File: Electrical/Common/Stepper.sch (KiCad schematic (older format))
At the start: 12 parts, among them Q301 FDC6420C

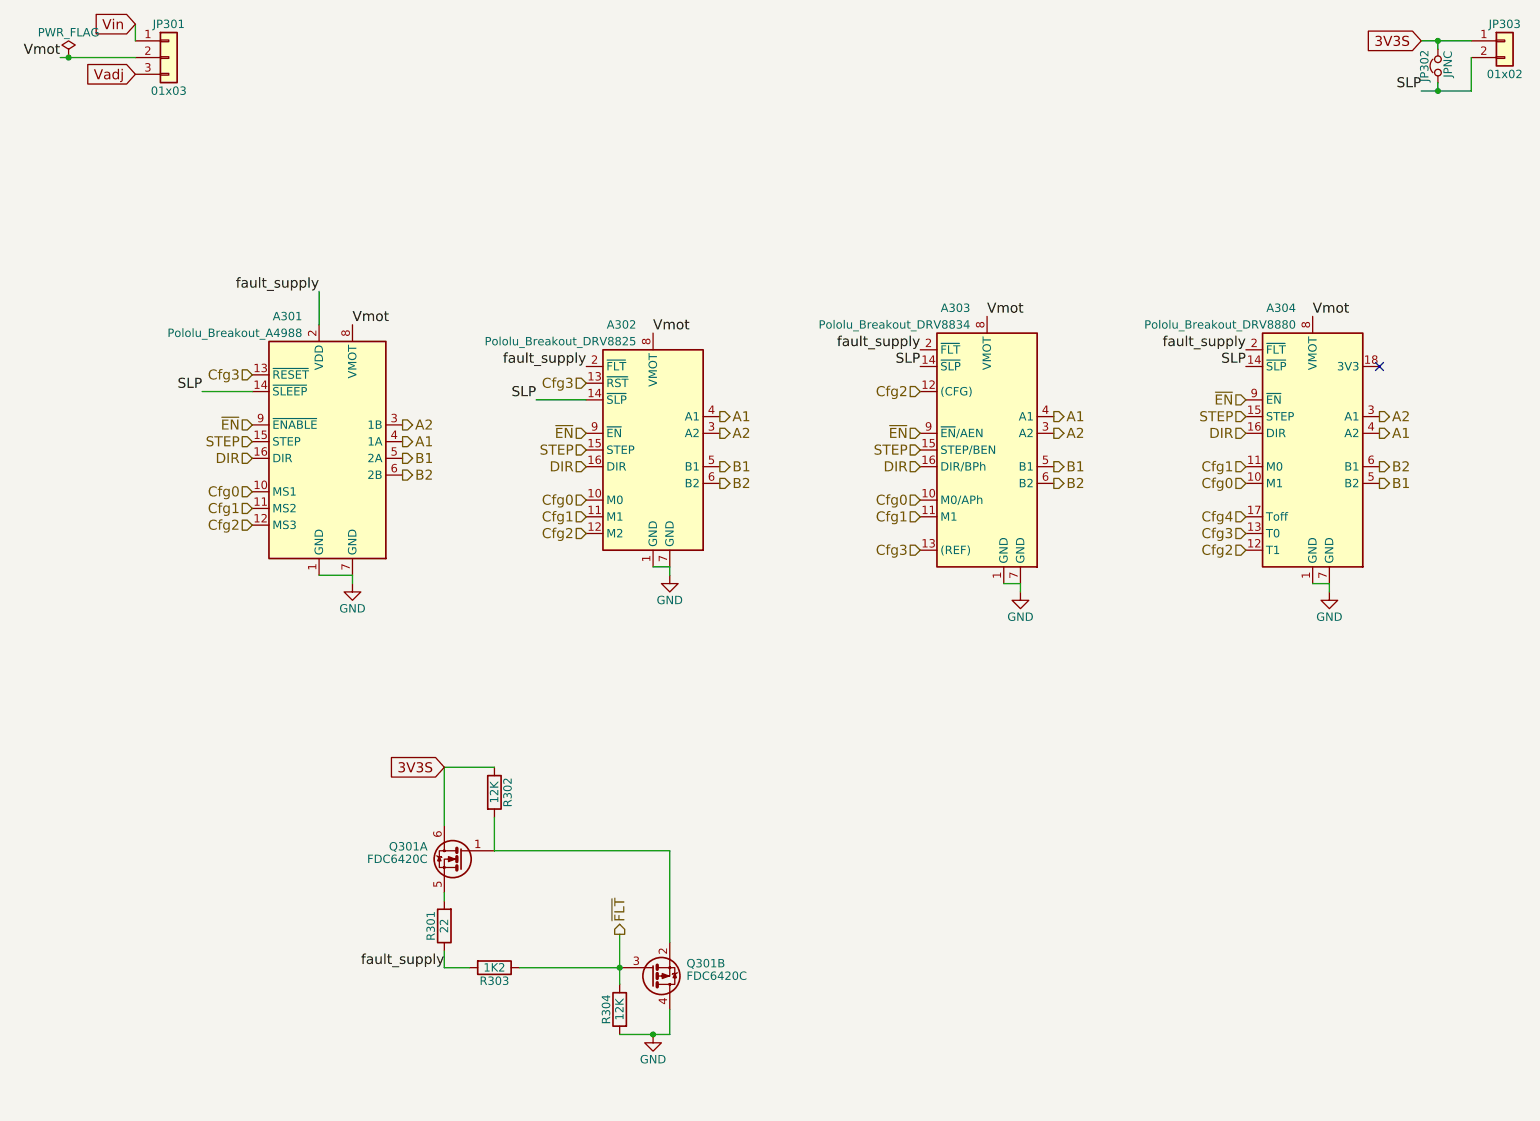
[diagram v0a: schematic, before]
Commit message: Completed Dual Stepper Layout. TODO: Via stitching.
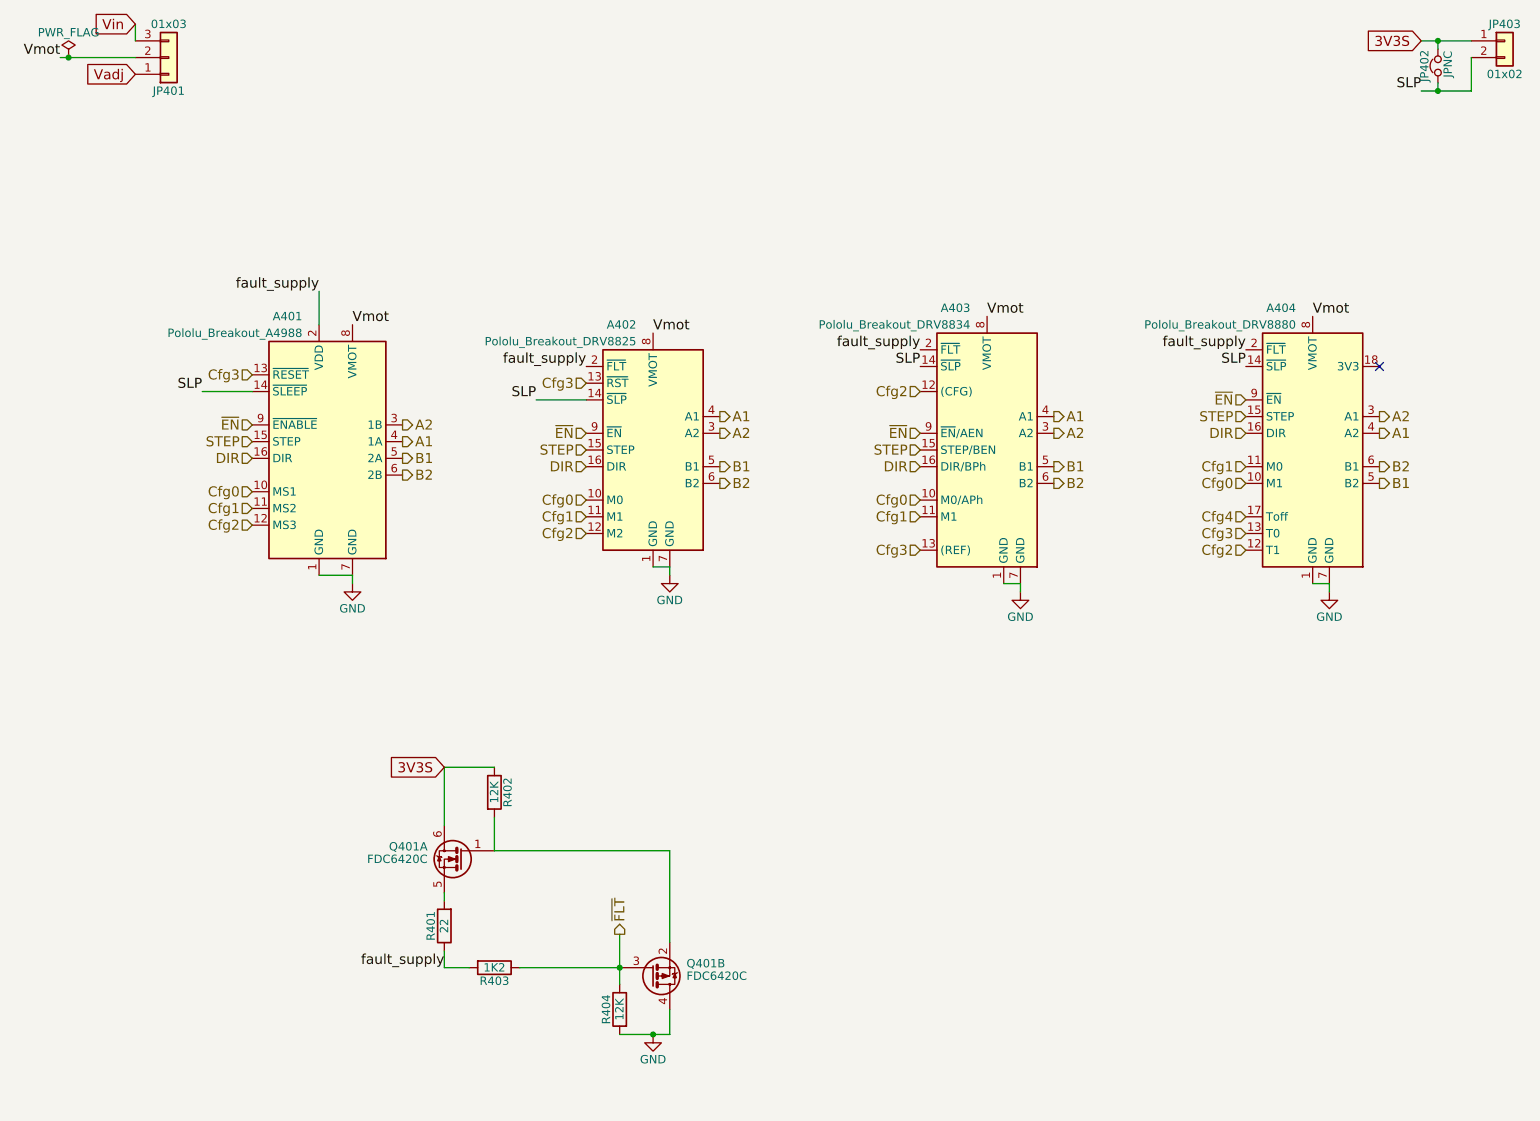
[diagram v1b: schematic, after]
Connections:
- net Vadj: now also JP301.1 (Pin_1); no longer JP301.3 (Pin_3)
- net Vin: now also JP301.3 (Pin_3); no longer JP301.1 (Pin_1)
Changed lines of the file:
@@
 $Descr A4 11693 8268
 encoding utf-8
-Sheet 3 4
+Sheet 4 4
 Title ""
 Date ""
@@
 AR Path="/5A5956FB/5A50EABF" Ref="A501"  Part="1"
 AR Path="/5A597FFD/5A50EABF" Ref="A601"  Part="1"
-F 0 "A301" H 2650 4200 50  0000 R CNN
+F 0 "A401" H 2650 4200 50  0000 R CNN
 F 1 "Pololu_Breakout_A4988" H 2650 4100 50  0000 R CNN
 F 2 "Modules:Pololu_Breakout-16_15.2x20.3mm" H 3025 2700 50  0001 L CNN
@@
 AR Path="/5A5956FB/5A50EB28" Ref="A502"  Part="1"
 AR Path="/5A597FFD/5A50EB28" Ref="A602"  Part="1"
-F 0 "A302" H 4650 4050 50  0000 R CNN
+F 0 "A402" H 4650 4050 50  0000 R CNN
 F 1 "Pololu_Breakout_DRV8825" H 4650 3950 50  0000 R CNN
 F 2 "Modules:Pololu_Breakout-16_15.2x20.3mm" H 4950 2600 50  0001 L CNN
@@
 AR Path="/5A5956FB/5A50F831" Ref="A503"  Part="1"
 AR Path="/5A597FFD/5A50F831" Ref="A603"  Part="1"
-F 0 "A303" H 6650 4350 50  0000 R CNN
+F 0 "A403" H 6650 4350 50  0000 R CNN
 F 1 "Pololu_Breakout_DRV8834" H 6650 4250 50  0000 R CNN
 F 2 "Modules:Pololu_Breakout-16_15.2x20.3mm" H 6950 2700 50  0001 L CNN
@@
 AR Path="/5A5956FB/5A50F8CE" Ref="A504"  Part="1"
 AR Path="/5A597FFD/5A50F8CE" Ref="A604"  Part="1"
-F 0 "A304" H 8600 4350 50  0000 R CNN
+F 0 "A404" H 8600 4350 50  0000 R CNN
 F 1 "Pololu_Breakout_DRV8880" H 8600 4250 50  0000 R CNN
 F 2 "footprints:Pololu_Breakout-17_15.2x20.3mm" H 8900 2700 50  0001 L CNN
@@
 DIR
 $Comp
-L GND #PWR040
+L GND #PWR041
 U 1 1 5A50FF78
 P 8800 4350
-AR Path="/5A579457/5A50EA77/5A50FF78" Ref="#PWR040"  Part="1"
-AR Path="/5A579457/5A569D3F/5A50FF78" Ref="#PWR046"  Part="1"
+AR Path="/5A579457/5A50EA77/5A50FF78" Ref="#PWR041"  Part="1"
+AR Path="/5A579457/5A569D3F/5A50FF78" Ref="#PWR047"  Part="1"
 AR Path="/5A5956FB/5A50FF78" Ref="#PWR051"  Part="1"
 AR Path="/5A597FFD/5A50FF78" Ref="#PWR057"  Part="1"
-F 0 "#PWR040" H 8800 4100 50  0001 C CNN
+F 0 "#PWR047" H 8800 4100 50  0001 C CNN
 F 1 "GND" H 8800 4200 50  0000 C CNN
 F 2 "" H 8800 4350 50  0001 C CNN
@@
 	8800 4300 8700 4300
 $Comp
-L GND #PWR041
+L GND #PWR042
 U 1 1 5A50FFB9
 P 6950 4350
-AR Path="/5A579457/5A50EA77/5A50FFB9" Ref="#PWR041"  Part="1"
-AR Path="/5A579457/5A569D3F/5A50FFB9" Ref="#PWR047"  Part="1"
+AR Path="/5A579457/5A50EA77/5A50FFB9" Ref="#PWR042"  Part="1"
+AR Path="/5A579457/5A569D3F/5A50FFB9" Ref="#PWR048"  Part="1"
 AR Path="/5A5956FB/5A50FFB9" Ref="#PWR052"  Part="1"
 AR Path="/5A597FFD/5A50FFB9" Ref="#PWR058"  Part="1"
-F 0 "#PWR041" H 6950 4100 50  0001 C CNN
+F 0 "#PWR048" H 6950 4100 50  0001 C CNN
 F 1 "GND" H 6950 4200 50  0000 C CNN
 F 2 "" H 6950 4350 50  0001 C CNN
@@
 $EndComp
 $Comp
-L GND #PWR042
+L GND #PWR043
 U 1 1 5A50FFD0
 P 4850 4250
-AR Path="/5A579457/5A50EA77/5A50FFD0" Ref="#PWR042"  Part="1"
-AR Path="/5A579457/5A569D3F/5A50FFD0" Ref="#PWR048"  Part="1"
+AR Path="/5A579457/5A50EA77/5A50FFD0" Ref="#PWR043"  Part="1"
+AR Path="/5A579457/5A569D3F/5A50FFD0" Ref="#PWR049"  Part="1"
 AR Path="/5A5956FB/5A50FFD0" Ref="#PWR053"  Part="1"
 AR Path="/5A597FFD/5A50FFD0" Ref="#PWR059"  Part="1"
-F 0 "#PWR042" H 4850 4000 50  0001 C CNN
+F 0 "#PWR049" H 4850 4000 50  0001 C CNN
 F 1 "GND" H 4850 4100 50  0000 C CNN
 F 2 "" H 4850 4250 50  0001 C CNN
@@
 $EndComp
 $Comp
-L GND #PWR043
+L GND #PWR044
 U 1 1 5A57FC8B
 P 2950 4300
-AR Path="/5A579457/5A50EA77/5A57FC8B" Ref="#PWR043"  Part="1"
-AR Path="/5A579457/5A569D3F/5A57FC8B" Ref="#PWR049"  Part="1"
+AR Path="/5A579457/5A50EA77/5A57FC8B" Ref="#PWR044"  Part="1"
+AR Path="/5A579457/5A569D3F/5A57FC8B" Ref="#PWR050"  Part="1"
 AR Path="/5A5956FB/5A57FC8B" Ref="#PWR054"  Part="1"
 AR Path="/5A597FFD/5A57FC8B" Ref="#PWR060"  Part="1"
-F 0 "#PWR043" H 2950 4050 50  0001 C CNN
+F 0 "#PWR050" H 2950 4050 50  0001 C CNN
 F 1 "GND" H 2950 4150 50  0000 C CNN
 F 2 "" H 2950 4300 50  0001 C CNN
@@
 AR Path="/5A5956FB/5A57FC8C" Ref="JP501"  Part="1"
 AR Path="/5A597FFD/5A57FC8C" Ref="JP601"  Part="1"
-F 0 "JP301" H 1850 1350 50  0000 C CNN
+F 0 "JP401" H 1850 1350 50  0000 C CNN
 F 1 "01x03" H 1850 950 50  0000 C CNN
 F 2 "Pin_Headers:Pin_Header_Straight_1x03_Pitch2.54mm" H 1850 1150 50  0001 C CNN
 F 3 "" H 1850 1150 50  0001 C CNN
 	1    1850 1150
-	1    0    0    -1
+	1    0    0    1
 $EndComp
 Wire Wire Line
@@
 AR Path="/5A5956FB/5A57FC8D" Ref="JP503"  Part="1"
 AR Path="/5A597FFD/5A57FC8D" Ref="JP603"  Part="1"
-F 0 "JP303" H 9850 1150 50  0000 C CNN
+F 0 "JP403" H 9850 1150 50  0000 C CNN
 F 1 "01x02" H 9850 850 50  0000 C CNN
 F 2 "Pin_Headers:Pin_Header_Straight_1x02_Pitch2.54mm" H 9850 1050 50  0001 C CNN
@@
 AR Path="/5A5956FB/5A57FC8E" Ref="Q501"  Part="2"
 AR Path="/5A597FFD/5A57FC8E" Ref="Q601"  Part="2"
-F 0 "Q301" H 4950 6725 50  0000 L CNN
+F 0 "Q401" H 4950 6725 50  0000 L CNN
 F 1 "FDC6420C" H 4950 6650 50  0000 L CNN
 F 2 "TO_SOT_Packages_SMD:SOT-363_SC-70-6" H 4950 6575 50  0001 L CIN
@@
 AR Path="/5A5956FB/5A57FC8F" Ref="Q501"  Part="1"
 AR Path="/5A597FFD/5A57FC8F" Ref="Q601"  Part="1"
-F 0 "Q301" H 3800 6025 50  0000 L CNN
+F 0 "Q401" H 3800 6025 50  0000 L CNN
 F 1 "FDC6420C" H 3800 5950 50  0000 L CNN
 F 2 "TO_SOT_Packages_SMD:SOT-363_SC-70-6" H 3800 5875 50  0001 L CIN
@@
 AR Path="/5A5956FB/5A559FB3" Ref="R502"  Part="1"
 AR Path="/5A597FFD/5A559FB3" Ref="R602"  Part="1"
-F 0 "R302" V 3880 5550 50  0000 C CNN
+F 0 "R402" V 3880 5550 50  0000 C CNN
 F 1 "12K" V 3800 5550 50  0000 C CNN
 F 2 "Resistors_SMD:R_0603_HandSoldering" V 3730 5550 50  0001 C CNN
@@
 AR Path="/5A5956FB/5A55A014" Ref="R504"  Part="1"
 AR Path="/5A597FFD/5A55A014" Ref="R604"  Part="1"
-F 0 "R304" V 4630 6850 50  0000 C CNN
+F 0 "R404" V 4630 6850 50  0000 C CNN
 F 1 "12K" V 4550 6850 50  0000 C CNN
 F 2 "Resistors_SMD:R_0603_HandSoldering" V 4480 6850 50  0001 C CNN
@@
 AR Path="/5A5956FB/5A55A0AD" Ref="R503"  Part="1"
 AR Path="/5A597FFD/5A55A0AD" Ref="R603"  Part="1"
-F 0 "R303" V 3880 6600 50  0000 C CNN
+F 0 "R403" V 3880 6600 50  0000 C CNN
 F 1 "1K2" V 3800 6600 50  0000 C CNN
 F 2 "Resistors_SMD:R_0603_HandSoldering" V 3730 6600 50  0001 C CNN
@@
 Connection ~ 4550 6600
 $Comp
-L GND #PWR044
+L GND #PWR045
 U 1 1 5A55A389
 P 4750 7000
-AR Path="/5A579457/5A50EA77/5A55A389" Ref="#PWR044"  Part="1"
-AR Path="/5A579457/5A569D3F/5A55A389" Ref="#PWR050"  Part="1"
+AR Path="/5A579457/5A50EA77/5A55A389" Ref="#PWR045"  Part="1"
+AR Path="/5A579457/5A569D3F/5A55A389" Ref="#PWR051"  Part="1"
 AR Path="/5A5956FB/5A55A389" Ref="#PWR055"  Part="1"
 AR Path="/5A597FFD/5A55A389" Ref="#PWR061"  Part="1"
-F 0 "#PWR044" H 4750 6750 50  0001 C CNN
+F 0 "#PWR051" H 4750 6750 50  0001 C CNN
 F 1 "GND" H 4750 6850 50  0000 C CNN
 F 2 "" H 4750 7000 50  0001 C CNN
@@
 AR Path="/5A5956FB/5A57FC94" Ref="R501"  Part="1"
 AR Path="/5A597FFD/5A57FC94" Ref="R601"  Part="1"
-F 0 "R301" V 3580 6350 50  0000 C CNN
+F 0 "R401" V 3580 6350 50  0000 C CNN
 F 1 "22" V 3500 6350 50  0000 C CNN
 F 2 "Resistors_SMD:R_0603_HandSoldering" V 3430 6350 50  0001 C CNN
@@
 AR Path="/5A5956FB/5A55DB5B" Ref="JP502"  Part="1"
 AR Path="/5A597FFD/5A55DB5B" Ref="JP602"  Part="1"
-F 0 "JP302" H 9450 1280 50  0000 C CNN
+F 0 "JP402" H 9450 1280 50  0000 C CNN
 F 1 "JPNC" H 9460 1140 50  0000 C CNN
 F 2 "footprints:JPNC" H 9450 1200 50  0001 C CNN
@@
 Cfg0
 $Comp
-L PWR_FLAG #FLG045
+L PWR_FLAG #FLG046
 U 1 1 5A59046B
 P 1250 1150
-AR Path="/5A579457/5A50EA77/5A59046B" Ref="#FLG045"  Part="1"
-AR Path="/5A579457/5A569D3F/5A59046B" Ref="#FLG051"  Part="1"
+AR Path="/5A579457/5A50EA77/5A59046B" Ref="#FLG046"  Part="1"
+AR Path="/5A579457/5A569D3F/5A59046B" Ref="#FLG052"  Part="1"
 AR Path="/5A5956FB/5A59046B" Ref="#FLG056"  Part="1"
 AR Path="/5A597FFD/5A59046B" Ref="#FLG062"  Part="1"
-F 0 "#FLG045" H 1250 1225 50  0001 C CNN
+F 0 "#FLG052" H 1250 1225 50  0001 C CNN
 F 1 "PWR_FLAG" H 1250 1300 50  0000 C CNN
 F 2 "" H 1250 1150 50  0001 C CNN
